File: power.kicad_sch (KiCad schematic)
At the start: 29 parts, among them J7 Conn_01x02, Q1 CSD17311Q5, Q2 CSD17311Q5, Q4 2N7002K, U10 DS4432U+, U8 INA260, U9 TPS40305

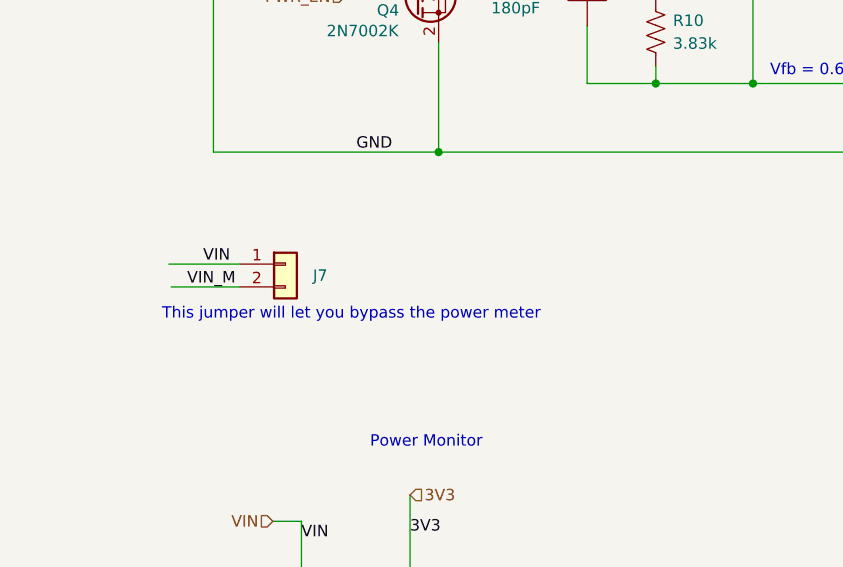
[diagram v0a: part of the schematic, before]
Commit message: Power analysis; updates to 205pd
Started analysis based on the 204 with an architecture diagram and with an smath document. Copied over manually changes from the 205 branch and started updating the schematic with USB PD capabilities. Only added decoy USB PD chip (CH224K), still need to fix power supplies.
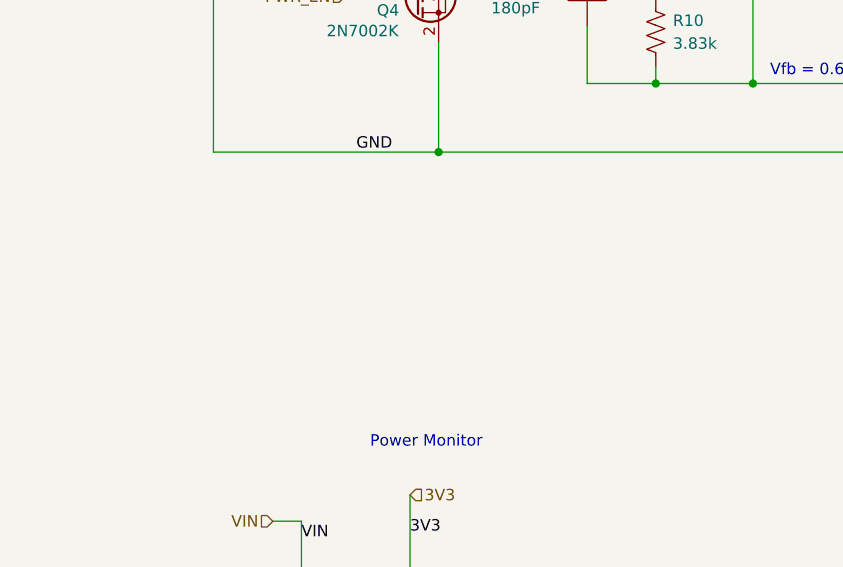
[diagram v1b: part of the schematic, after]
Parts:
- removed J7: Conn_01x02, Connector_PinHeader_2.54mm:PinHeader_1x02_P2.54mm_Vertical, symbol Connector_Generic:Conn_01x02
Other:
- note removed: "This jumper will let you bypass the power meter"
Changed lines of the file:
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@@
   (title_block
     (title "Bitaxe Ultra")
-    (date "2023-12-10")
-    (rev "204")
+    (date "2023-12-15")
+    (rev "205")
   )
   (junction (at 135.89 116.84) (diameter 0) (color 0 0 0 0)
@@
     (stroke (width 0) (type default))
   )
-  (wire (pts (xy 41.402 93.726) (xy 49.022 93.726))
-    (stroke (width 0) (type default))
-  )
   (wire (pts (xy 157.48 67.31) (xy 170.18 67.31))
     (stroke (width 0) (type default))
@@
   )
   (wire (pts (xy 201.93 59.69) (xy 201.93 61.595))
-    (stroke (width 0) (type default))
-  )
-  (wire (pts (xy 41.148 91.186) (xy 49.022 91.186))
     (stroke (width 0) (type default))
   )
@@
     (effects (font (size 1.27 1.27)) (justify left bottom))
   )
-  (text "This jumper will let you bypass the power meter" (at 40.386 97.536 0)
-    (effects (font (size 1.27 1.27)) (justify left bottom))
-  )
   (label "3V3" (at 203.835 111.125 0) (fields_autoplaced)
     (effects (font (size 1.27 1.27)) (justify left bottom))
@@
   )
   (label "GND" (at 61.976 78.74 0) (fields_autoplaced)
-    (effects (font (size 1.27 1.27)) (justify left bottom))
-  )
-  (label "VIN" (at 44.958 91.186 0) (fields_autoplaced)
     (effects (font (size 1.27 1.27)) (justify left bottom))
   )
@@
   )
   (label "GND" (at 223.52 137.795 0) (fields_autoplaced)
-    (effects (font (size 1.27 1.27)) (justify left bottom))
-  )
-  (label "VIN_M" (at 43.18 93.726 0) (fields_autoplaced)
     (effects (font (size 1.27 1.27)) (justify left bottom))
   )
@@
         )
       )
-    )
-  )
-  (symbol (lib_id "Connector_Generic:Conn_01x02") (at 54.102 91.186 0) (unit 1)
-    (in_bom no) (on_board yes) (dnp no) (fields_autoplaced)
-    (property "Reference" "J7" (at 57.15 92.4559 0)
-      (effects (font (size 1.27 1.27)) (justify left))
-    )
-    (property "Value" "Conn_01x02" (at 57.15 93.7259 0)
-      (effects (font (size 1.27 1.27)) (justify left) hide)
-    )
-    (property "Footprint" "Connector_PinHeader_2.54mm:PinHeader_1x02_P2.54mm_Vertical" (at 54.102 91.186 0)
-      (effects (font (size 1.27 1.27)) hide)
-    )
-    (property "Datasheet" "~" (at 54.102 91.186 0)
-      (effects (font (size 1.27 1.27)) hide)
-    )
-    (pin "1")
-    (pin "2")
-    (instances
-      (project "bitaxeUltra"
-        (path "/e63e39d7-6ac0-4ffd-8aa3-1841a4541b55/8ec0a9c6-2b78-44ef-a83d-9047d2828409"
-          (reference "J7") (unit 1)
-        )
-      )

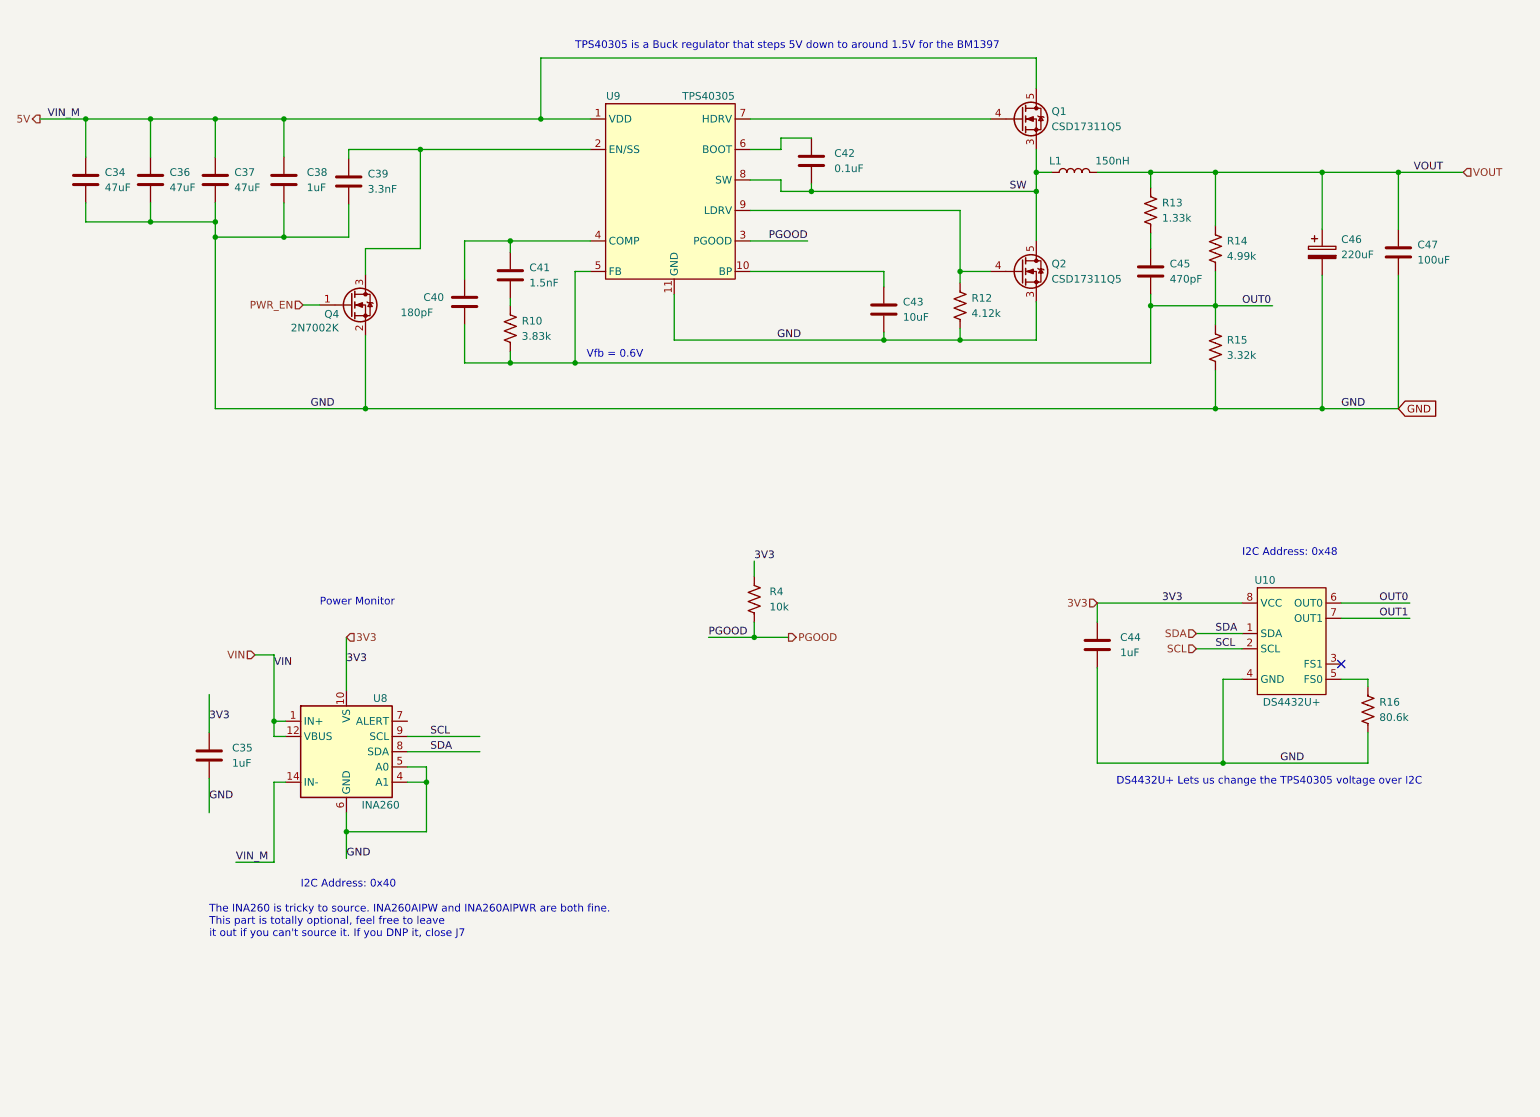
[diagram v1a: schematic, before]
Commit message: Worked on VDD
Started importing SiC431A for VDD supply. Yet to do Vfb, Mode, Pgood, boot, phase, en. Moved power supplies to power page. Configured CH224K to 12V
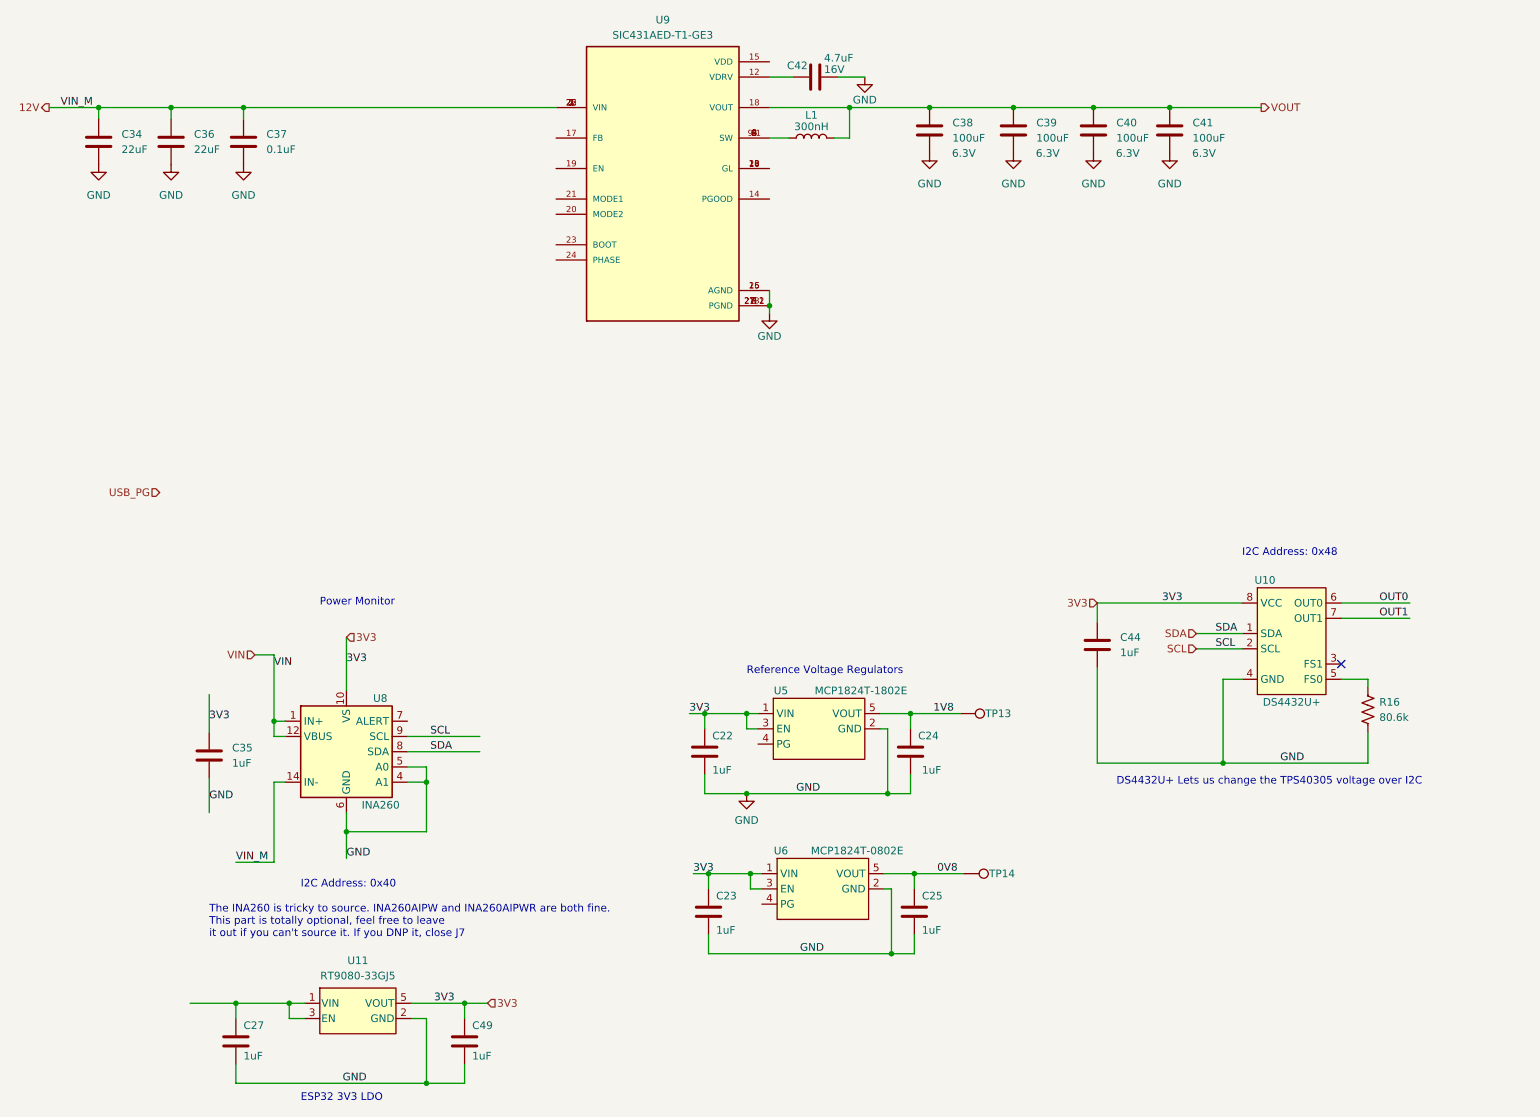
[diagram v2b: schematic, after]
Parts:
- removed C43: 10uF, Capacitor_SMD:C_0805_2012Metric, symbol Device:C
- removed C45: 470pF, Capacitor_SMD:C_0805_2012Metric, symbol Device:C
- removed C46: 220uF, bitaxe:CAP_2R5TPE220MAFB, symbol Device:C_Polarized
- removed C47: 100uF, Capacitor_SMD:C_1206_3216Metric, symbol Device:C
- removed Q1, Q2: CSD17311Q5, bitaxe:CSD17311Q5, symbol bitaxe:Q_NMOS_CSD17311Q5_1
- removed Q4: 2N7002K, Package_TO_SOT_SMD:SOT-323_SC-70, symbol Transistor_FET:2N7002K
- removed R10: 3.83k, Resistor_SMD:R_0402_1005Metric, symbol Device:R_US
- removed R12: 4.12k, Resistor_SMD:R_0402_1005Metric, symbol Device:R_US
- removed R13: 1.33k, Resistor_SMD:R_0402_1005Metric, symbol Device:R_US
- removed R14: 4.99k, Resistor_SMD:R_0402_1005Metric, symbol Device:R_US
- removed R15: 3.32k, Resistor_SMD:R_0402_1005Metric, symbol Device:R_US
- removed R4: 10k, Resistor_SMD:R_0402_1005Metric, symbol Device:R_US
- removed U9: TPS40305, bitaxe:TPS40305, symbol bitaxe:TPS40305
- added C22, C23, C24, C25, C27, C49: 1uF, Capacitor_SMD:C_0402_1005Metric, symbol Device:C
- added TP13, TP14: TestPoint, TestPoint:TestPoint_Pad_D1.5mm, symbol Connector:TestPoint
- added U11: RT9080-33GJ5, bitaxe:RT9080-33GJ5, symbol bitaxe:RT9080-33GJ5
- added U5: MCP1824T-1802E, Package_TO_SOT_SMD:SOT-23-5, symbol bitaxe:MCP1824
- added U6: MCP1824T-0802E, Package_TO_SOT_SMD:SOT-23-5, symbol bitaxe:MCP1824
- added U9: SIC431AED-T1-GE3, bitaxe:REGULATOR_SIC431AED-T1-GE3, symbol bitaxe:SIC431AED-T1-GE3
- C34, C36: value 47uF -> 22uF; DK 490-6539-1-ND -> 1276-3392-1-ND; PARTNO GRM32ER61C476KE15L -> CL32B226KAJNNNE
- C37: value 47uF -> 0.1uF; footprint Capacitor_SMD:C_1210_3225Metric -> Capacitor_SMD:C_0402_1005Metric; DK 490-6539-1-ND -> 1276-6720-1-ND; PARTNO GRM32ER61C476KE15L -> CL05B104KA5NNNC
- C38: value 1uF -> 100uF; footprint Capacitor_SMD:C_0805_2012Metric -> Capacitor_SMD:C_1206_3216Metric; DK 1276-6471-1-ND -> 490-GRM31CD80J107MEA8KCT-ND; PARTNO CL21B105KOFNNNG -> GRM31CD80J107MEA8K; Voltage (none) -> 6.3V
- C39: value 3.3nF -> 100uF; footprint Capacitor_SMD:C_0402_1005Metric -> Capacitor_SMD:C_1206_3216Metric; DK 1276-1552-1-ND -> 490-GRM31CD80J107MEA8KCT-ND; PARTNO CL05B332KB5NNNC -> GRM31CD80J107MEA8K; Voltage (none) -> 6.3V
- C40: value 180pF -> 100uF; footprint Capacitor_SMD:C_0805_2012Metric -> Capacitor_SMD:C_1206_3216Metric; DK 311-1114-1-ND -> 490-GRM31CD80J107MEA8KCT-ND; PARTNO CC0805JRNPO9BN181 -> GRM31CD80J107MEA8K; Voltage (none) -> 6.3V
- C41: value 1.5nF -> 100uF; footprint Capacitor_SMD:C_0805_2012Metric -> Capacitor_SMD:C_1206_3216Metric; DK 311-1128-1-ND -> 490-GRM31CD80J107MEA8KCT-ND; PARTNO CC0805KRX7R9BB152 -> GRM31CD80J107MEA8K; Voltage (none) -> 6.3V
- C42: value 0.1uF -> 4.7uF; footprint Capacitor_SMD:C_0402_1005Metric -> Capacitor_SMD:C_0805_2012Metric; DK 1292-1639-1-ND -> 490-GRM21BR71C475KE51KCT-ND; PARTNO 0402X104K100CT -> GRM21BR71C475KE51K; Voltage (none) -> 16V
- L1: value 150nH -> 300nH; footprint bitaxe:FP1005R1-R15-R -> bitaxe:INDUCTOR_SPB1007-R30M; DK 513-1568-1-ND -> (none); PARTNO FP1005R1-R15-R -> (none)
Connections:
- net 3V3: now also C22.1, C23.1, C49.1, U11.5 (VOUT), U5.1 (VIN), U5.3 (EN), U6.1 (VIN), U6.3 (EN)
- net GND: now also C40.2, C41.2, C42.2, C22.2, C23.2, C24.2, C25.2, C27.2, C49.2, U11.2 (GND), U5.2 (GND), U6.2 (GND), U9.13 (PGND), U9.16 (AGND), U9.25 (AGND), U9.27_1 (PGND), U9.27_2 (PGND), U9.3 (PGND), U9.4 (PGND)
- net OUT0: no longer C40.2
- net VOUT: now also C38.1, C39.1, C40.1, C41.1, U9.18 (VOUT)
- net at C42.1: now also U9.12 (VDRV)
- net 5V renamed 12V
- net 12V: now also U9.1 (VIN), U9.2 (VIN), U9.22 (VIN), U9.26 (VIN); no longer C38.1
- net SW: no longer names the net of L1.1
- net SW: now also U9.5 (SW), U9.6 (SW), U9.7 (SW), U9.8 (SW), U9.9 (SW), U9.9.1 (SW); no longer C42.2
- new net: C27.1, U11.1 (VIN), U11.3 (EN)
- new net: U9.10 (GL), U9.11 (GL), U9.28 (GL)
- new net 0V8: C25.1, TP14.1, U6.5 (VOUT)
- new net 1V8: C24.1, TP13.1, U5.5 (VOUT)
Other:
- note added: "ESP32 3V3 LDO"
- note added: "Reference Voltage Regulators"
- note removed: "TPS40305 is a Buck regulator that steps 5V down to around 1.5V for the BM1397"
- note removed: "Vfb = 0.6V"
